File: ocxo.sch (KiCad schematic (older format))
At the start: 21 parts, among them J1 Conn_01x02, J2 Conn_01x01, J3 Conn_Coaxial, J4 Conn_01x01, J5 Conn_01x01, J6 Conn_01x01, J7 Conn_Coaxial, Q1 ENE3311 OCXO, U1 KA78M05_TO252, U2 LM4140

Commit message: minor bug fixed
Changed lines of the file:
@@
 U 1 1 5A0B6442
 P 4250 2000
-F 0 "RV1" V 4075 2000 50  0000 C CNN
+F 0 "RV1" V 4250 2000 50  0000 C CNN
 F 1 "5k" V 4150 2000 50  0000 C CNN
 F 2 "Potentiometers:Potentiometer_Trimmer_Vishay_43" H 4250 2000 50  0001 C CNN
@@
 U 1 1 5A0B664E
 P 4800 2000
-F 0 "C4" H 4810 2070 50  0000 L CNN
+F 0 "C4" V 4950 1950 50  0000 L CNN
 F 1 "10n" H 4810 1920 50  0000 L CNN
 F 2 "Capacitors_SMD:C_0805_HandSoldering" H 4800 2000 50  0001 C CNN
@@
 U 1 1 5A425F65
 P 4050 2000
-F 0 "RV2" V 3875 2000 50  0000 C CNN
+F 0 "RV2" V 4050 2000 50  0000 C CNN
 F 1 "5k" V 3950 2000 50  0000 C CNN
 F 2 "Potentiometers:Potentiometer_Trimmer_Bourns_3299Y" H 4050 2000 50  0001 C CNN
@@
 U 1 1 5A426460
 P 4550 2000
-F 0 "RV3" V 4375 2000 50  0000 C CNN
-F 1 "5k" V 4450 2000 50  0000 C CNN
+F 0 "RV3" V 4550 2000 50  0000 C CNN
+F 1 "5k" V 4450 1950 50  0000 C CNN
 F 2 "Potentiometers:Potentiometer_Trimmer_Bourns_3299W" H 4550 2000 50  0001 C CNN
 F 3 "" H 4550 2000 50  0001 C CNN

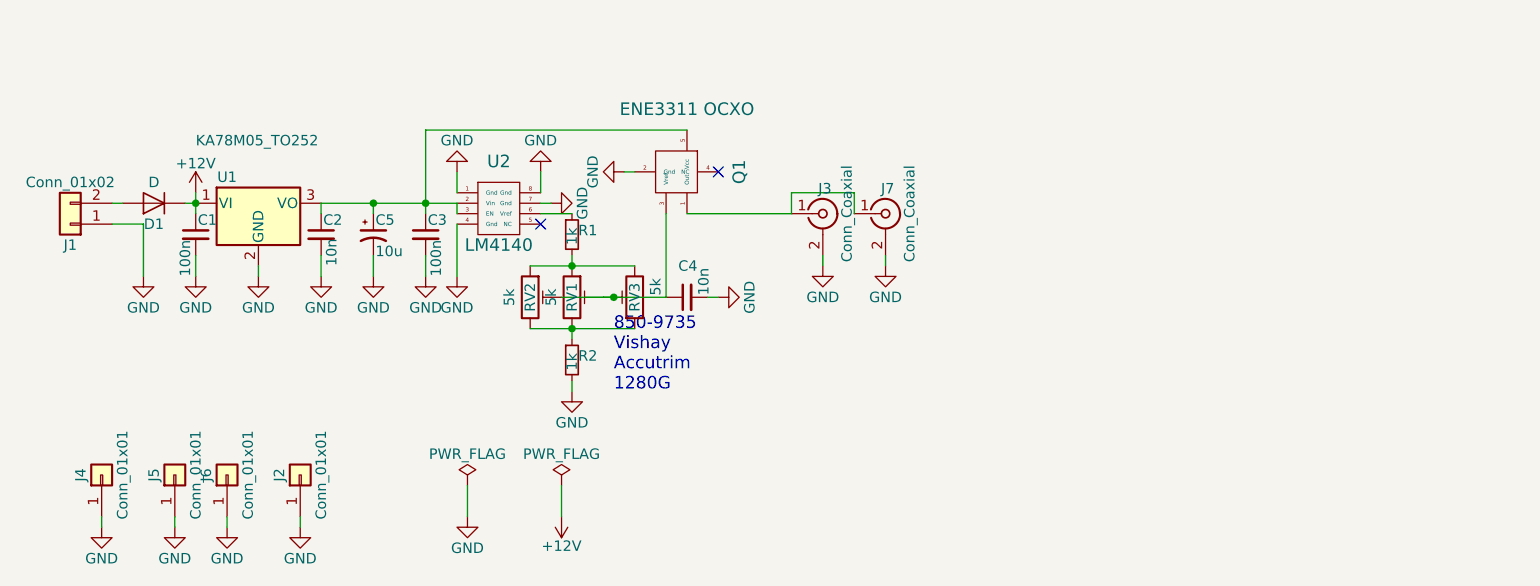
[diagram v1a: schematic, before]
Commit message: added output voltage for LM4140
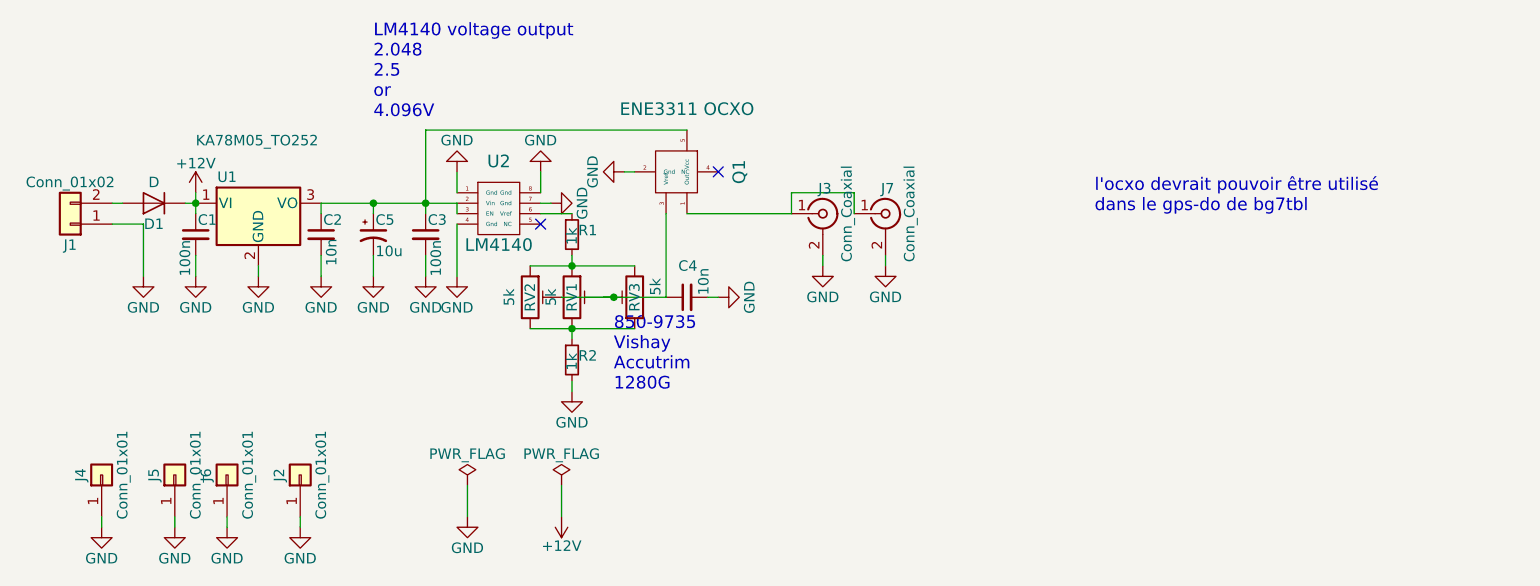
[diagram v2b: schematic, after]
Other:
- note added: "LM4140 voltage output\n2.048\n2.5\nor \n4.096V \n"
- note added: "l'ocxo devrait pouvoir être utilisé \ndans le gps-do de bg7tbl"
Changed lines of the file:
@@
 Connection ~ 4250 1850
 Connection ~ 4250 2150
+Text Notes 6750 1600 0    60   ~ 0
+l'ocxo devrait pouvoir être utilisé \ndans le gps-do de bg7tbl
+Text Notes 3300 1150 0    60   ~ 0
+LM4140 voltage output\n2.048\n2.5\nor \n4.096V \n
 $EndSCHEMATC

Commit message: upgrade to Kicad 5.x
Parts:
- C1, C2, C3, C4: symbol C_Small -> ocxo-rescue:C_Small
- C5: symbol CP1_Small -> ocxo-rescue:CP1_Small
- D1: symbol D -> ocxo-rescue:D
- J1: symbol Conn_01x02 -> ocxo-rescue:Conn_01x02
- J2, J4, J5, J6: symbol Conn_01x01 -> ocxo-rescue:Conn_01x01
- J3, J7: symbol Conn_Coaxial -> ocxo-rescue:Conn_Coaxial
- Q1: symbol ENE3311 -> ene3311:ENE3311
- R1, R2: symbol R_Small -> ocxo-rescue:R_Small
- RV1, RV2, RV3: symbol POT_TRIM -> ocxo-rescue:POT_TRIM
- U1: symbol KA78M05_TO252 -> ocxo-rescue:KA78M05_TO252
- U2: symbol LM4140 -> lm4140:LM4140
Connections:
- net at C4.1, Q1.3 (Vref), RV2.2: no longer RV1.2, RV3.2
- new net: RV1.2, RV3.2
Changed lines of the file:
@@
-EESchema Schematic File Version 2
-LIBS:power
-LIBS:device
-LIBS:conn
-LIBS:regul
-LIBS:ene3311
-LIBS:lm4140
+EESchema Schematic File Version 4
 LIBS:ocxo-cache
-EELAYER 25 0
+EELAYER 26 0
 EELAYER END
 $Descr A4 11693 8268
@@
 $EndDescr
 $Comp
-L KA78M05_TO252 U1
+L ocxo-rescue:KA78M05_TO252 U1
 U 1 1 5A0B59D5
 P 2750 1550
@@
 $EndComp
 $Comp
-L ENE3311 Q1
+L ene3311:ENE3311 Q1
 U 1 1 5A0B5BA5
 P 4700 1400
@@
 $EndComp
 $Comp
-L LM4140 U2
+L lm4140:LM4140 U2
 U 1 1 5A0B5C08
 P 3900 1550
@@
 $EndComp
 $Comp
-L C_Small C2
+L ocxo-rescue:C_Small C2
 U 1 1 5A0B5D01
 P 3050 1700
@@
 $EndComp
 $Comp
-L C_Small C3
+L ocxo-rescue:C_Small C3
 U 1 1 5A0B5D26
 P 3550 1700
@@
 $EndComp
 Wire Wire Line
-	3050 1550 3700 1550
+	3050 1550 3300 1550
 Wire Wire Line
 	3050 1550 3050 1600
 Wire Wire Line
-	3550 1200 3550 1600
+	3550 1200 3550 1550
 Connection ~ 3550 1550
 $Comp
-L C_Small C1
+L ocxo-rescue:C_Small C1
 U 1 1 5A0B5D91
 P 2450 1700
@@
 $EndComp
 Wire Wire Line
-	2450 1500 2450 1600
-$Comp
-L GND #PWR01
+	2450 1500 2450 1550
+$Comp
+L ocxo-rescue:GND #PWR01
 U 1 1 5A0B5E73
 P 3750 3050
@@
 $EndComp
 $Comp
-L PWR_FLAG #FLG02
+L ocxo-rescue:PWR_FLAG #FLG02
 U 1 1 5A0B5E93
 P 3750 2900
@@
 $EndComp
 $Comp
-L +12V #PWR03
+L ocxo-rescue:+12V #PWR03
 U 1 1 5A0B5EB3
 P 4200 3050
@@
 $EndComp
 $Comp
-L +12V #PWR04
+L ocxo-rescue:+12V #PWR04
 U 1 1 5A0B5F1F
 P 2450 1500
@@
 Connection ~ 2450 1550
 $Comp
-L GND #PWR05
+L ocxo-rescue:GND #PWR05
 U 1 1 5A0B5FE5
 P 3700 1900
@@
 $EndComp
 $Comp
-L GND #PWR06
+L ocxo-rescue:GND #PWR06
 U 1 1 5A0B6003
 P 2450 1900
@@
 $EndComp
 $Comp
-L GND #PWR07
+L ocxo-rescue:GND #PWR07
 U 1 1 5A0B605B
 P 3050 1900
@@
 $EndComp
 $Comp
-L GND #PWR08
+L ocxo-rescue:GND #PWR08
 U 1 1 5A0B6067
 P 3550 1900
@@
 $EndComp
 $Comp
-L GND #PWR09
+L ocxo-rescue:GND #PWR09
 U 1 1 5A0B6085
 P 3700 1400
@@
 $EndComp
 $Comp
-L GND #PWR010
+L ocxo-rescue:GND #PWR010
 U 1 1 5A0B60BF
 P 4100 1400
@@
 $EndComp
 $Comp
-L GND #PWR011
+L ocxo-rescue:GND #PWR011
 U 1 1 5A0B60CB
 P 4150 1550
@@
 	3050 1800 3050 1900
 $Comp
-L GND #PWR012
+L ocxo-rescue:GND #PWR012
 U 1 1 5A0B617D
 P 2750 1900
@@
 	4800 1600 5300 1600
 $Comp
-L GND #PWR013
+L ocxo-rescue:GND #PWR013
 U 1 1 5A0B6281
 P 4500 1400
@@
 	4550 1400 4500 1400
 $Comp
-L R_Small R1
+L ocxo-rescue:R_Small R1
 U 1 1 5A0B62ED
 P 4250 1700
@@
 $EndComp
 $Comp
-L R_Small R2
+L ocxo-rescue:R_Small R2
 U 1 1 5A0B6431
 P 4250 2300
@@
 $EndComp
 $Comp
-L POT_TRIM RV1
+L ocxo-rescue:POT_TRIM RV1
 U 1 1 5A0B6442
 P 4250 2000
@@
 	4250 2150 4250 2200
 $Comp
-L GND #PWR014
+L ocxo-rescue:GND #PWR014
 U 1 1 5A0B65AA
 P 4250 2450
@@
 	4250 2400 4250 2450
 Wire Wire Line
-	4400 2000 4700 2000
-Wire Wire Line
 	4700 2000 4700 1600
 $Comp
-L C_Small C4
+L ocxo-rescue:C_Small C4
 U 1 1 5A0B664E
 P 4800 2000
@@
 $EndComp
 $Comp
-L GND #PWR015
+L ocxo-rescue:GND #PWR015
 U 1 1 5A0B6654
 P 4950 2000
@@
 NoConn ~ 4950 1400
 $Comp
-L GND #PWR016
+L ocxo-rescue:GND #PWR016
 U 1 1 5A0B670A
 P 2200 1900
@@
 $EndComp
 $Comp
-L GND #PWR017
+L ocxo-rescue:GND #PWR017
 U 1 1 5A0B671A
 P 5450 1850
@@
 	2200 1650 2050 1650
 $Comp
-L Conn_01x01 J2
+L ocxo-rescue:Conn_01x01 J2
 U 1 1 5A0B6837
 P 2950 2850
@@
 $EndComp
 $Comp
-L GND #PWR018
+L ocxo-rescue:GND #PWR018
 U 1 1 5A0B68EF
 P 2950 3100
@@
 	2950 3050 2950 3100
 $Comp
-L PWR_FLAG #FLG019
+L ocxo-rescue:PWR_FLAG #FLG019
 U 1 1 5A0B69E5
 P 4200 2900
@@
 	2450 1800 2450 1900
 $Comp
-L Conn_Coaxial J3
+L ocxo-rescue:Conn_Coaxial J3
 U 1 1 5A0B6BE9
 P 5450 1600
@@
 	5450 1800 5450 1850
 $Comp
-L Conn_01x02 J1
+L ocxo-rescue:Conn_01x02 J1
 U 1 1 5A0B6CF6
 P 1850 1650
@@
 $EndComp
 $Comp
-L D D1
+L ocxo-rescue:D D1
 U 1 1 5A0B6D3B
 P 2250 1550
@@
 850-9735\nVishay \nAccutrim \n1280G\n\n
 $Comp
-L CP1_Small C5
+L ocxo-rescue:CP1_Small C5
 U 1 1 5A4114C5
 P 3300 1700
@@
 $EndComp
 $Comp
-L GND #PWR020
+L ocxo-rescue:GND #PWR020
 U 1 1 5A4115CB
 P 3300 1900
@@
 Connection ~ 3300 1550
 $Comp
-L GND #PWR021
+L ocxo-rescue:GND #PWR021
 U 1 1 5A412389
 P 5750 1850
@@
 $EndComp
 $Comp
-L Conn_Coaxial J7
+L ocxo-rescue:Conn_Coaxial J7
 U 1 1 5A41238F
 P 5750 1600
@@
 	5300 1500 5300 1600
 $Comp
-L Conn_01x01 J6
+L ocxo-rescue:Conn_01x01 J6
 U 1 1 5A41248C
 P 2600 2850
@@
 $EndComp
 $Comp
-L GND #PWR022
+L ocxo-rescue:GND #PWR022
 U 1 1 5A412492
 P 2600 3100
@@
 	2600 3050 2600 3100
 $Comp
-L Conn_01x01 J5
+L ocxo-rescue:Conn_01x01 J5
 U 1 1 5A412515
 P 2350 2850
@@
 $EndComp
 $Comp
-L GND #PWR023
+L ocxo-rescue:GND #PWR023
 U 1 1 5A41251B
 P 2350 3100
@@
 	2350 3050 2350 3100
 $Comp
-L Conn_01x01 J4
+L ocxo-rescue:Conn_01x01 J4
 U 1 1 5A412522
 P 2000 2850
@@
 $EndComp
 $Comp
-L GND #PWR024
+L ocxo-rescue:GND #PWR024
 U 1 1 5A412528
 P 2000 3100
@@
 	2000 3050 2000 3100
 $Comp
-L POT_TRIM RV2
+L ocxo-rescue:POT_TRIM RV2
 U 1 1 5A425F65
 P 4050 2000
@@
 $EndComp
 Wire Wire Line
-	4050 1850 4550 1850
-Wire Wire Line
-	4050 2150 4550 2150
-Wire Wire Line
-	4200 2000 4450 2000
-Connection ~ 4450 2000
-$Comp
-L POT_TRIM RV3
+	4050 1850 4250 1850
+Wire Wire Line
+	4050 2150 4250 2150
+$Comp
+L ocxo-rescue:POT_TRIM RV3
 U 1 1 5A426460
 P 4550 2000
@@
 Text Notes 3300 1150 0    60   ~ 0
 LM4140 voltage output\n2.048\n2.5\nor \n4.096V \n
+Wire Wire Line
+	3550 1550 3700 1550
+Wire Wire Line
+	3550 1550 3550 1600
+Wire Wire Line
+	2450 1550 2450 1600
+Wire Wire Line
+	3300 1550 3550 1550
+Wire Wire Line
+	4250 1850 4550 1850
+Wire Wire Line
+	4250 2150 4550 2150
+Wire Wire Line
+	4200 2000 4700 2000
 $EndSCHEMATC
